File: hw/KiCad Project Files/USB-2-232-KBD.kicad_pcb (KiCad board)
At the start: 2 copper layers, 77.4 x 56 mm, 55 parts, among them J1 Conn_01x05_Male, J2 USB-PINHEADER, J3 Keyboard Pin put, J4 PWR-PINH, J5 Conn_01x02_Male, P1 Keyboard, P2 USB_B_Mini, P3 DB9_Female_MountingHoles, P4 USB_A, Q1 Q_NPN_BEC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

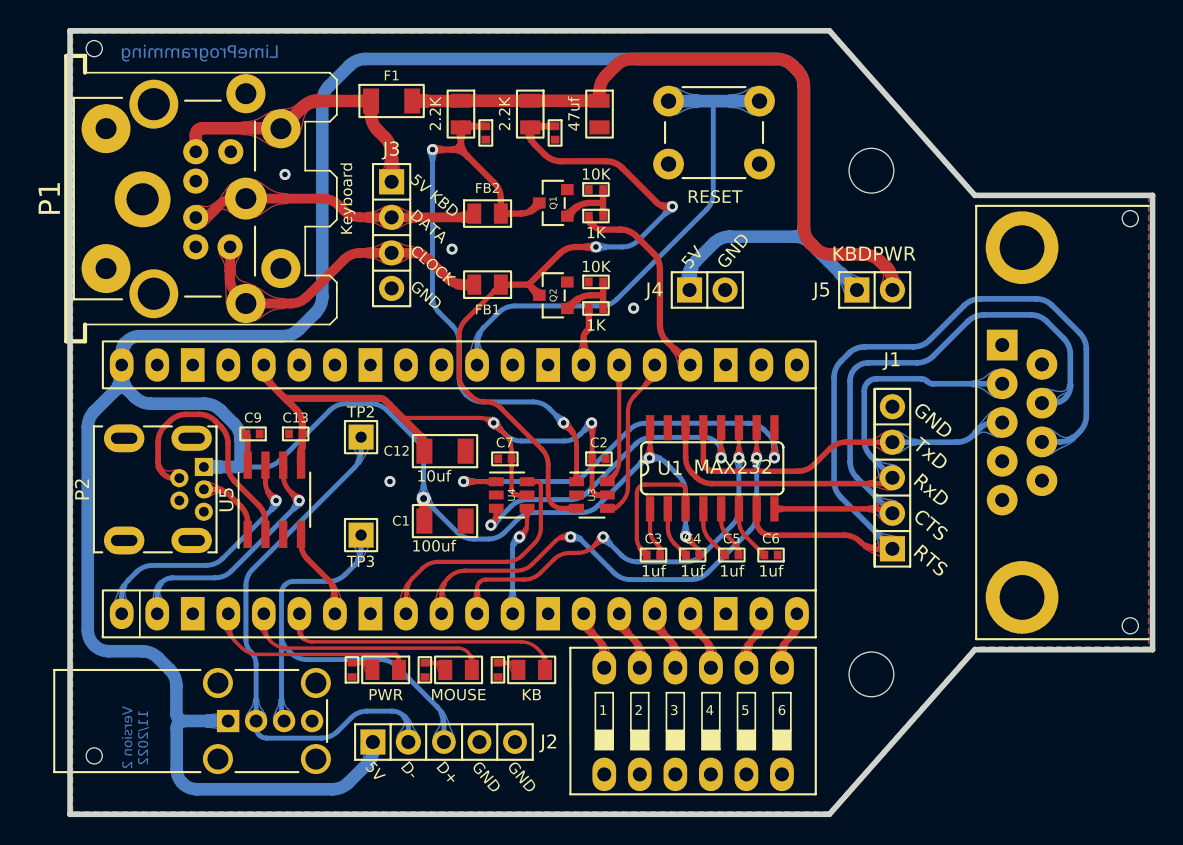
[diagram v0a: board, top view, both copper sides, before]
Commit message: Hardware update
Added a Bleed resistor. My AT machine has a bleed resistor of 150R, so I added a bleed resistor of 120K to the PCB. It shouldn't interfere with the keyboard controller nor add much to power draw but it will eventually drain the capacitors and that's all that really matters
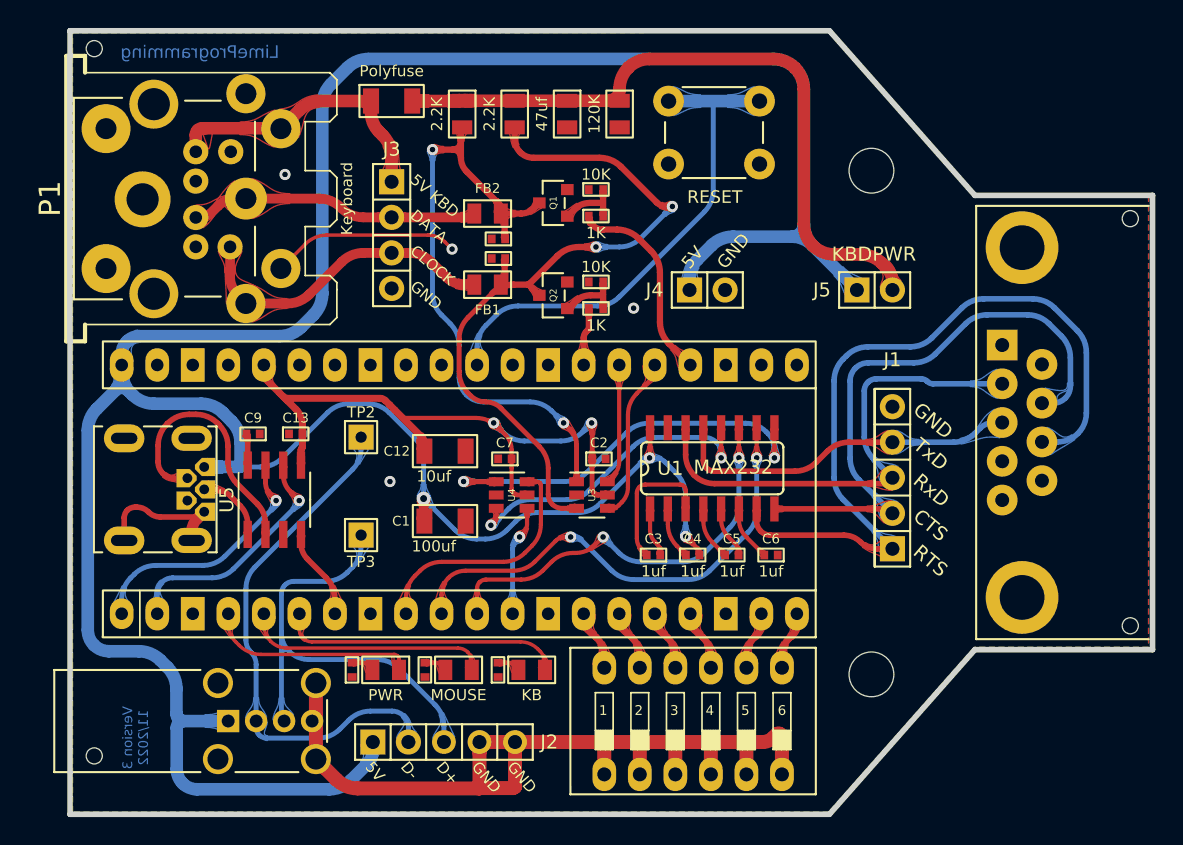
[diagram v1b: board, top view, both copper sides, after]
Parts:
- added R10: 120K, USB-2-232-KBD:R_0805_2012Metric, F.Cu at (147.0, 75.4)
- moved C10 9.85 mm to (138.3, 85.8), turned to 180 degrees
- moved C11 7.63 mm to (138.3, 84.3), turned to 180 degrees
- moved C8 2.31 mm to (143.2, 75.4)
- moved R8 1.11 mm to (139.5, 75.4)
- moved R7 0.09 mm to (135.8, 75.4)
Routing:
- net GND: track 0.00 -> 87.4 mm
- net Net-(C10-Pad1): track 52.0 -> 53.0 mm
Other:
- board text added: "Version 3 11/2022"
- board text removed: "Version 2 11/2022"
